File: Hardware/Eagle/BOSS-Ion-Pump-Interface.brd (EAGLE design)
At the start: 48.3 x 66 mm, 34 parts, among them J1 MOLEX-22112022, J2 MOLEX-22112042, J3 MOLEX-22112042, J4 MOLEX-22112062, U1 ISO224ADWVR, U2 ISO224ADWVR

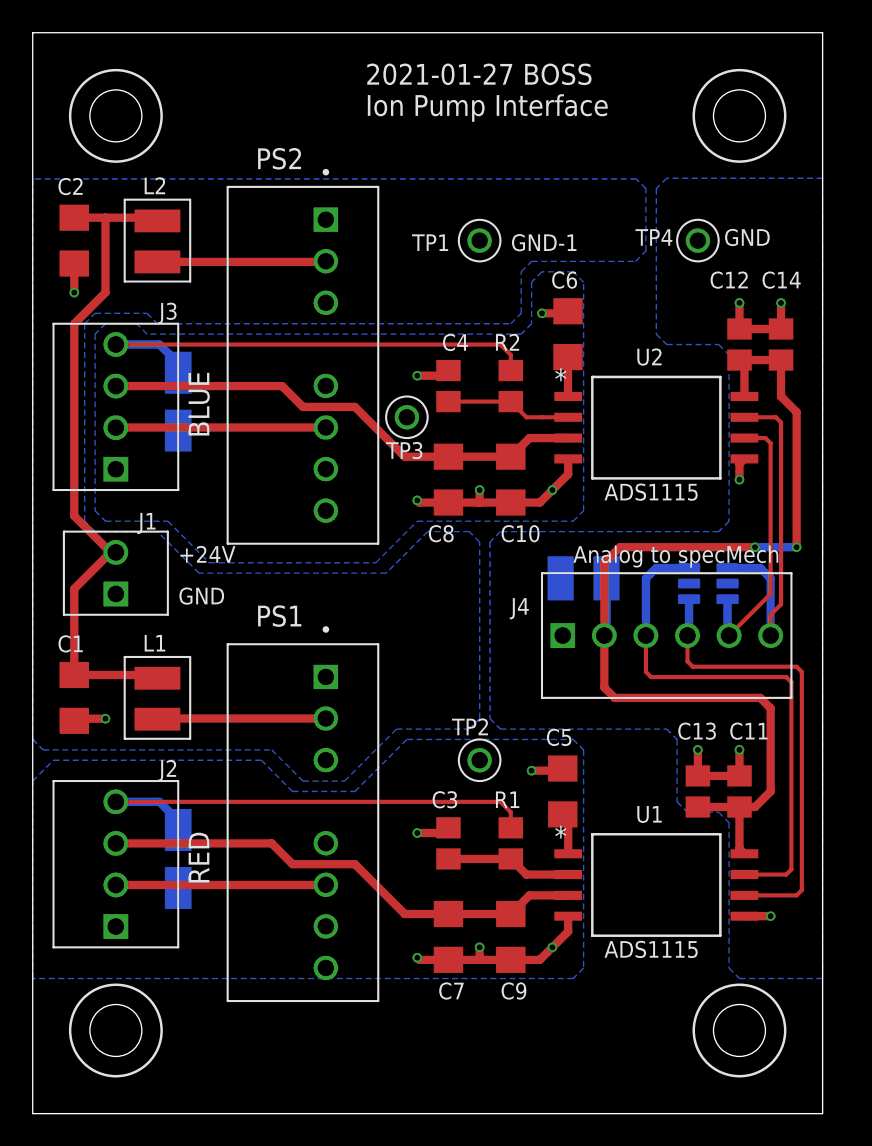
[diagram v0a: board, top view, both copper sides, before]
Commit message: Added reverse polarity protection
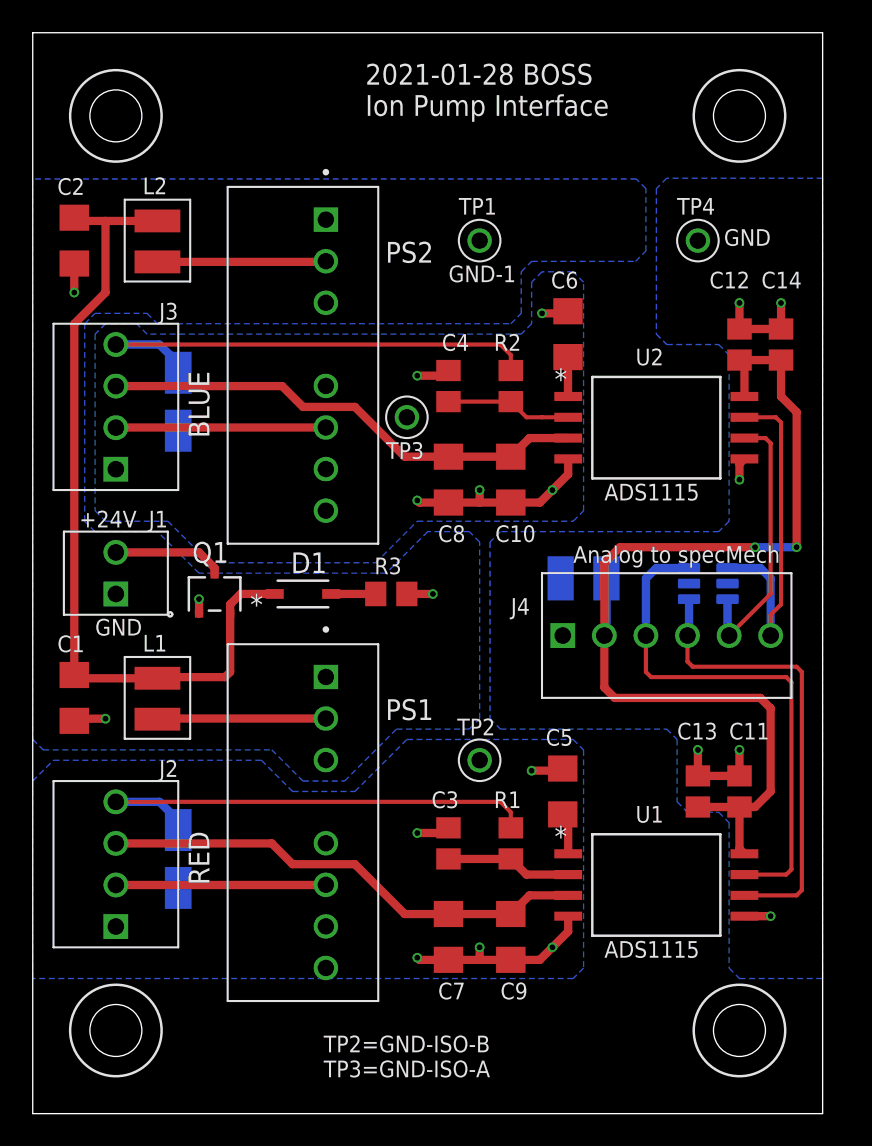
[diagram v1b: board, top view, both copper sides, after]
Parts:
- added D1: 11V, AUmlib:SOD123_DIO
- added Q1: SSM3J351R, AUmlib:SOT-23F_TOS
- added R3: 100K, AUmlib:R0805
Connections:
- new net +24V-PROT: C1.1, C2.1, D1.1, L1.1, L2.1, Q1.2
- new net N$2: D1.2, R3.2
- net +24V: now also Q1.3; no longer C1.1, C2.1, L1.1, L2.1
- net GND-1: now also Q1.1, R3.1
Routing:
- net +24V-PROT: track 0.00 -> 50.7 mm
- net +24V: track 41.2 -> 6.82 mm
- net N$2: track 0.00 -> 2.72 mm
- net GND-1: track 3.73 -> 6.20 mm, vias 2 -> 4
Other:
- board text added: "2021-01-28 BOSS Ion Pump Interface"
- board text added: "OUTN-A"
- board text added: "OUTN-B"
- board text added: "OUTP-A"
- board text added: "OUTP-B"
- board text added: "TP2=GND-ISO-B TP3=GND-ISO-A"
- board text removed: "2021-01-27 BOSS Ion Pump Interface"
- board text removed: "BLUE+"
- board text removed: "BLUE-"
- board text removed: "RED+"
- board text removed: "RED-"

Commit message: Changed TVS diode to 10 V from 6 V and labeled reverse polarity Zener
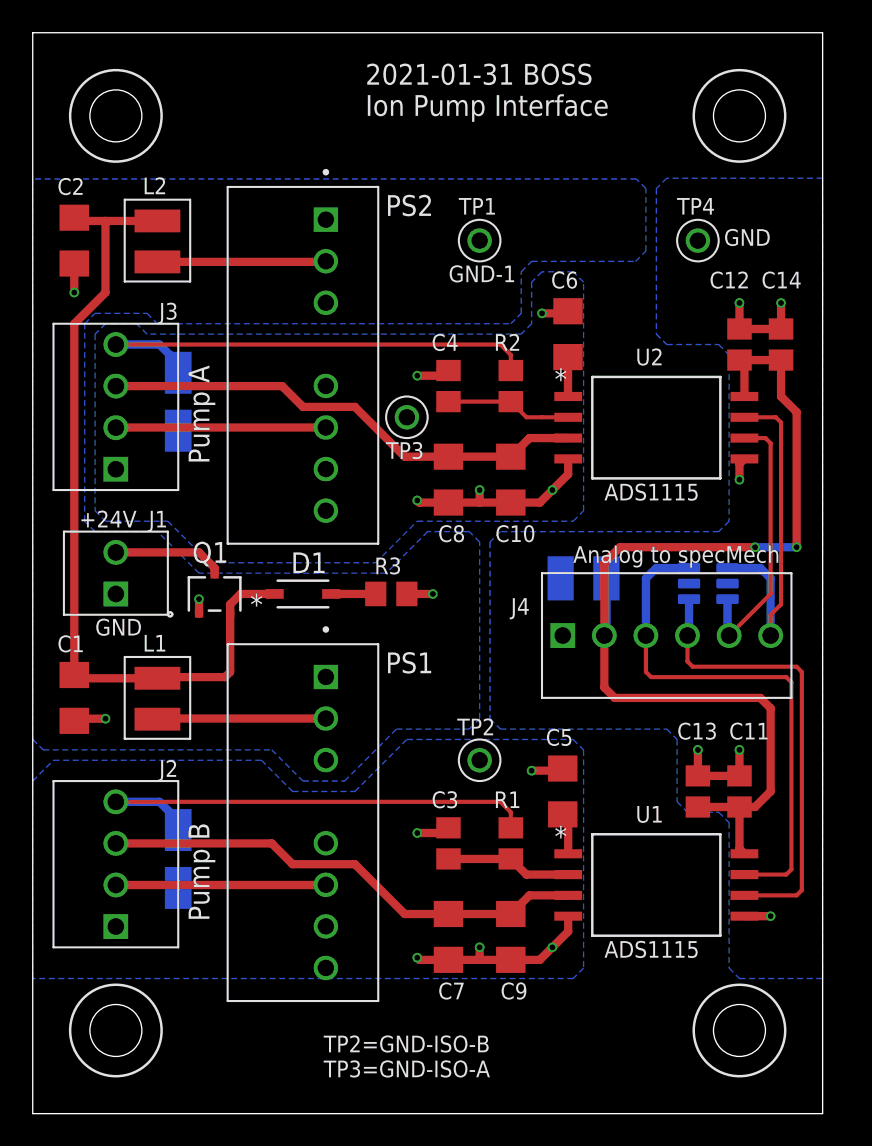
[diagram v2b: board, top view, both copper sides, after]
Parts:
- D1: value 11V -> BZT52C11-7-F
- TVS1, TVS2: value SMAJ6.0CA-13F -> SMAJ10CA-13F
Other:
- board text added: "2021-01-31 BOSS Ion Pump Interface"
- board text added: "GND-ISO-A"
- board text added: "GND-ISO-B"
- board text added: "Pump A"
- board text added: "Pump B"
- board text added: "VIN-A"
- board text added: "VIN-B"
- board text removed: "2021-01-28 BOSS Ion Pump Interface"
- board text removed: "BLUE"
- board text removed: "RED"

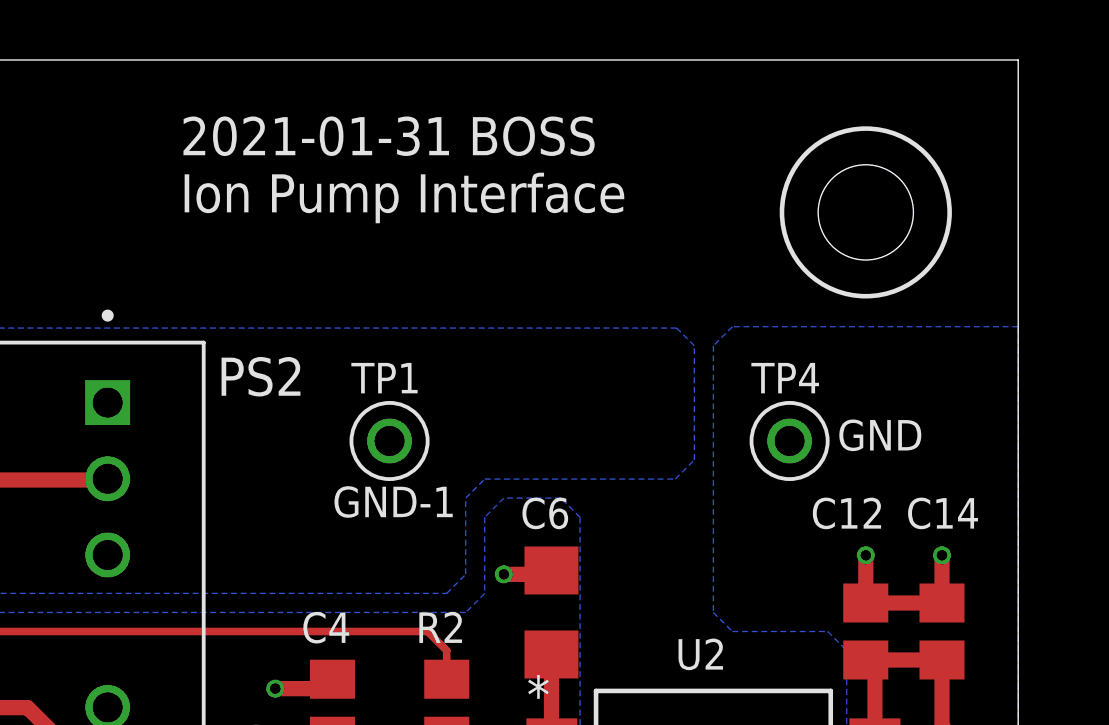
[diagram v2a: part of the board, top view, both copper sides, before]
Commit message: Added names to the reverse polarity zener net
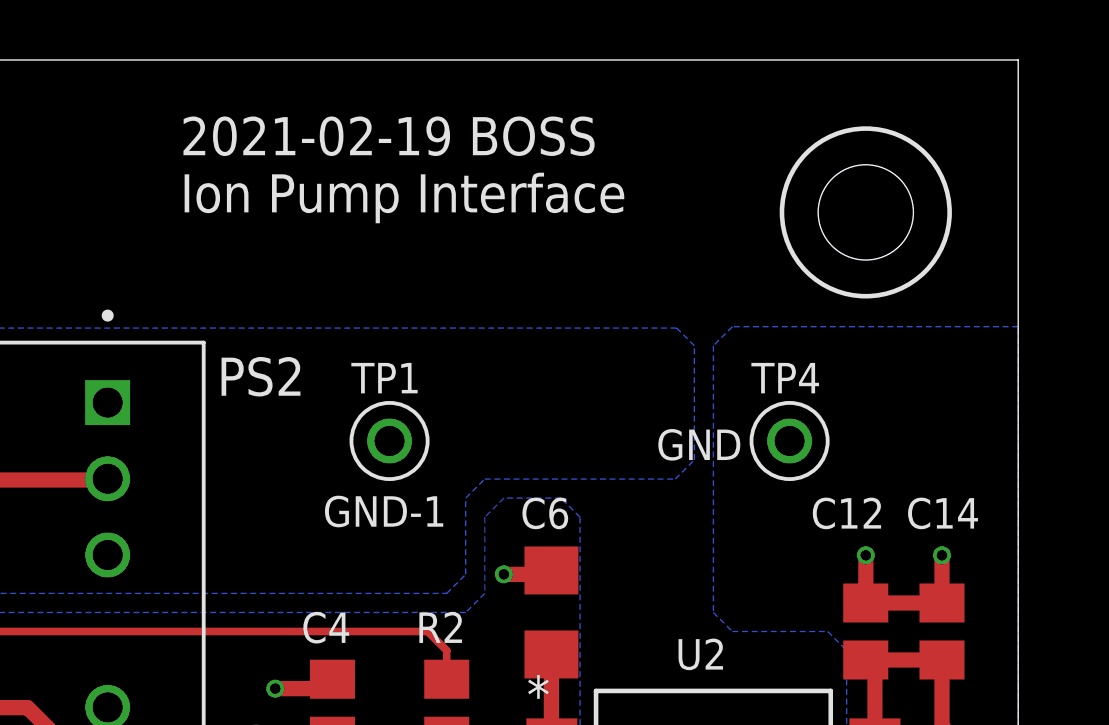
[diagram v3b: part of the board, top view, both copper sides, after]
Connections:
- net N$2 renamed REVERSE-POL-ZENER
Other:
- board text added: "2021-02-19 BOSS Ion Pump Interface"
- board text removed: "2021-01-31 BOSS Ion Pump Interface"
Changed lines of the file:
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@@
 <grid distance="0.0125" unitdist="inch" unit="inch" style="lines" multiple="1" display="yes" altdistance="5" altunitdist="mil" altunit="mil"/>
 <layers>
-<layer number="1" name="Top" color="4" fill="1" visible="no" active="yes"/>
+<layer number="1" name="Top" color="4" fill="1" visible="yes" active="yes"/>
 <layer number="2" name="Route2" color="16" fill="1" visible="no" active="no"/>
 <layer number="3" name="Route3" color="17" fill="1" visible="no" active="no"/>
@@
 <layer number="19" name="Unrouted" color="6" fill="1" visible="yes" active="yes"/>
 <layer number="20" name="Dimension" color="24" fill="1" visible="yes" active="yes"/>
-<layer number="21" name="tPlace" color="7" fill="1" visible="no" active="yes"/>
+<layer number="21" name="tPlace" color="7" fill="1" visible="yes" active="yes"/>
 <layer number="22" name="bPlace" color="7" fill="1" visible="yes" active="yes"/>
 <layer number="23" name="tOrigins" color="15" fill="1" visible="yes" active="yes"/>
@@
 <hole x="43.18" y="60.96" drill="3.175"/>
 <circle x="43.18" y="60.96" radius="2.794" width="0.1524" layer="21"/>
-<text x="20.32" y="60.96" size="1.27" layer="21">2021-01-31 BOSS
+<text x="20.32" y="60.96" size="1.27" layer="21">2021-02-19 BOSS
 Ion Pump Interface</text>
 <text x="41.91" y="22.225" size="1.016" layer="22" font="vector" rot="MR90">OUTN-A</text>
@@
 <text x="16.51" y="41.275" size="1.016" layer="22" font="vector" rot="MR0">+15V</text>
 <text x="16.51" y="13.335" size="1.016" layer="22" font="vector" rot="MR0">+15V</text>
-<text x="34.29" y="60.96" size="1.27" layer="22" rot="MR0">2021-01-31 BOSS
+<text x="34.29" y="60.96" size="1.27" layer="22" rot="MR0">2021-02-19 BOSS
 Ion Pump Interface</text>
-<text x="25.4" y="50.8" size="1.016" layer="21" font="vector">GND-1</text>
-<text x="42.2275" y="53.0225" size="1.016" layer="21" font="vector">GND</text>
+<text x="25.0825" y="50.4825" size="1.016" layer="21" font="vector">GND-1</text>
+<text x="36.195" y="52.705" size="1.016" layer="21" font="vector">GND</text>
 <text x="17.78" y="2.2225" size="1.016" layer="21">TP2=GND-ISO-B
 TP3=GND-ISO-A</text>
@@
 <wire x1="14.785" y1="31.75" x2="12.7" y2="31.75" width="0.508" layer="1"/>
 </signal>
-<signal name="N$2">
+<signal name="REVERSE-POL-ZENER">
 <contactref element="R3" pad="2"/>
 <contactref element="D1" pad="2"/>
